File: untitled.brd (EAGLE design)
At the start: 95.2 x 57.4 mm, 62 parts, among them IC1 SIM900, IC2 ST1S10PHR, IC3 SMF05C, IC5 BQ24072, IC6 SIM68R, X1 ST-SMB-H, X2 ST-SMB-H

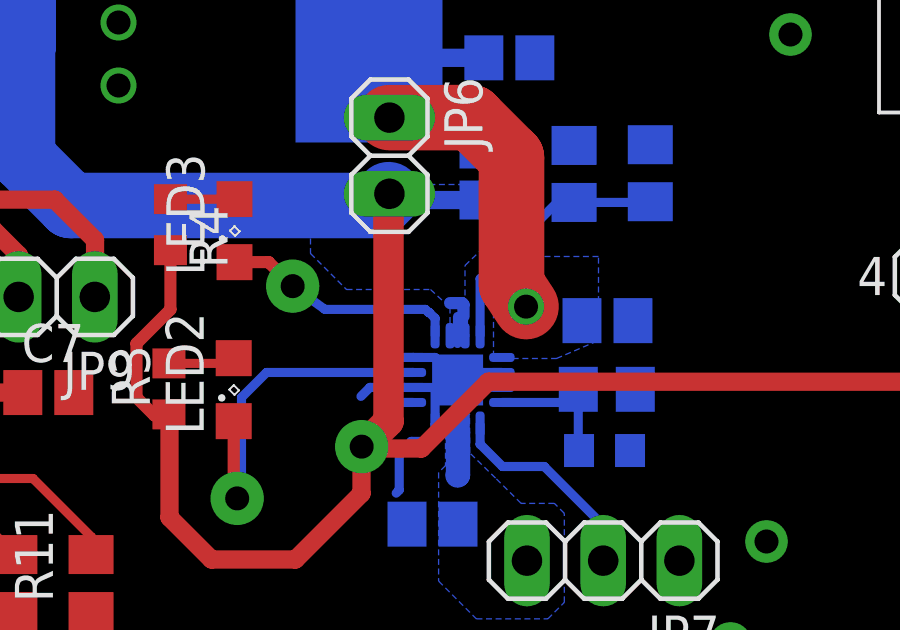
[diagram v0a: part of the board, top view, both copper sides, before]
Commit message: Supply changes
Some traces had been changed in power supply circuit
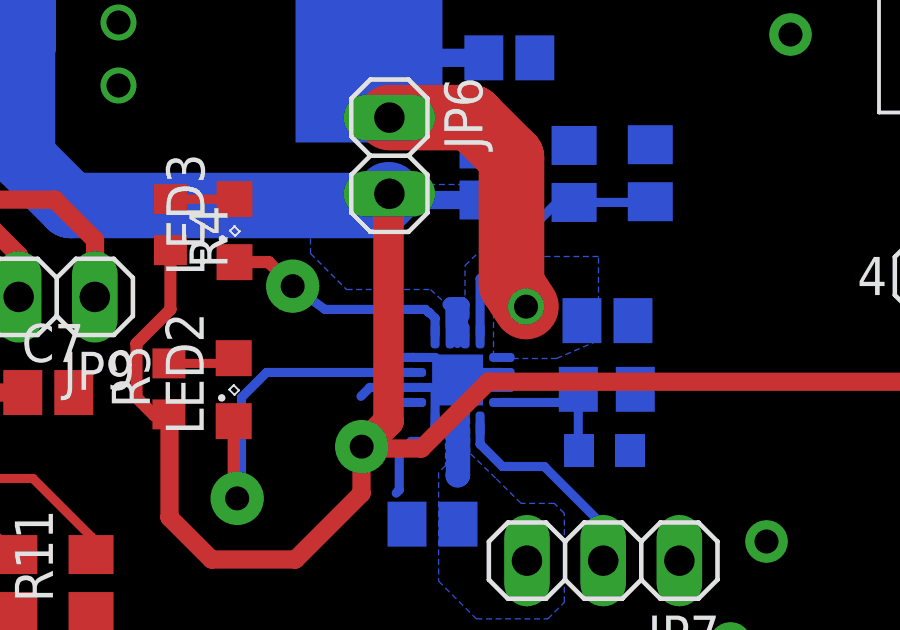
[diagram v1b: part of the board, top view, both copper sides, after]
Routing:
- net VBAT: track 150.0 -> 150.8 mm
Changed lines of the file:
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@@
 <wire x1="52" y1="13" x2="52" y2="14.556" width="0.6096" layer="1"/>
 <wire x1="52" y1="14.556" x2="52.006" y2="14.562" width="0.6096" layer="1"/>
-<wire x1="52.906" y1="22.962" x2="52.9" y2="22.9" width="0" layer="19" extent="1-16"/>
-<wire x1="52.931" y1="22.9895" x2="52.906" y2="22.962" width="0" layer="19" extent="16-16"/>
 <wire x1="54.9535" y1="19.3465" x2="55.3535" y2="19.3465" width="0.4064" layer="16"/>
 <wire x1="55.3535" y1="19.3465" x2="55.4" y2="19.3" width="0.4064" layer="16"/>
@@
 <wire x1="55.4535" y1="18.2595" x2="55.4" y2="18.2595" width="0.3048" layer="16"/>
 <wire x1="55.4" y1="18.2595" x2="55.4" y2="18.9" width="0.3048" layer="16"/>
+<wire x1="54.9" y1="19.3" x2="55" y2="19.3" width="0.4064" layer="16"/>
+<wire x1="55" y1="19.3" x2="55" y2="18.6" width="0.4064" layer="16"/>
+<wire x1="55" y1="18.6" x2="54.9535" y2="18.2595" width="0" layer="19" extent="16-16"/>
+<wire x1="52.906" y1="22.962" x2="52.931" y2="22.9895" width="0" layer="19" extent="16-16"/>
+<wire x1="52.9" y1="22.9" x2="52.906" y2="22.962" width="0" layer="19" extent="1-16"/>
 </signal>
 <signal name="N$5">

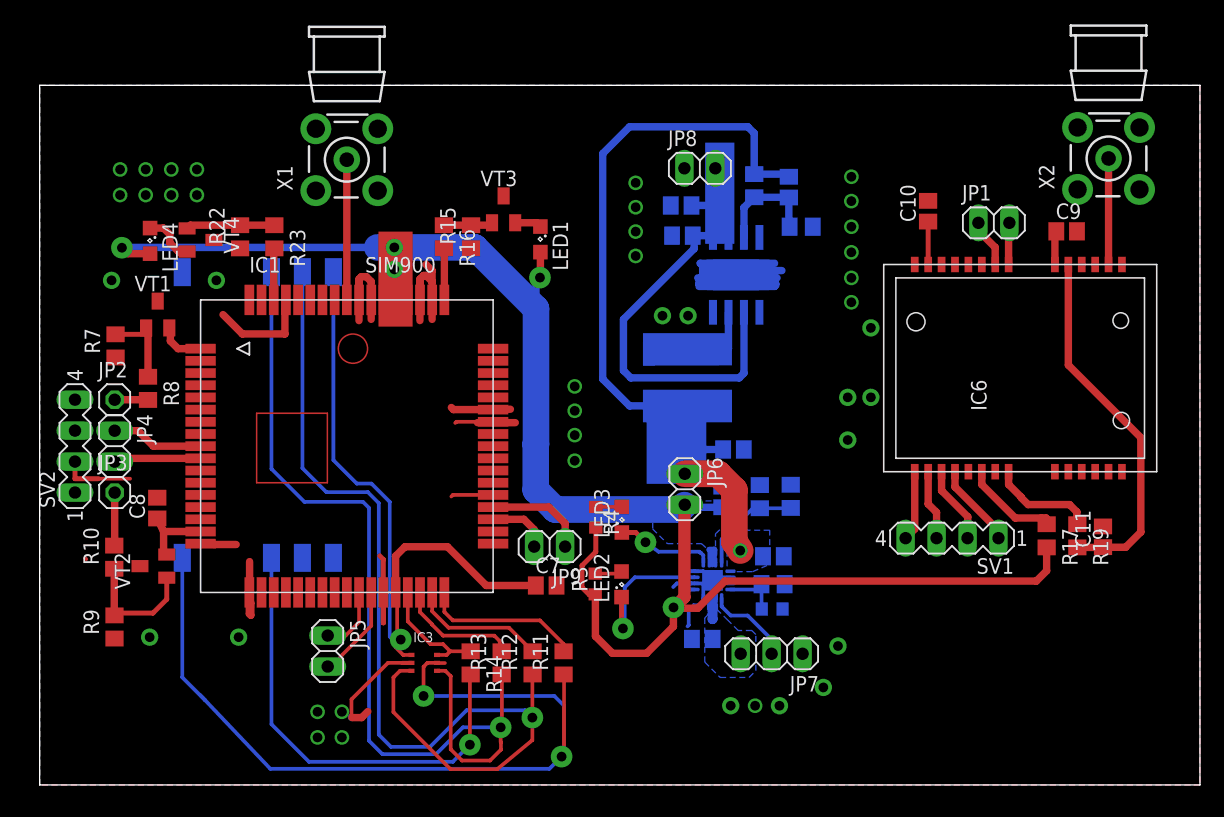
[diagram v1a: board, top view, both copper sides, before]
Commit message: Trace changes
Following items are changed:
- area between SIM900R and SIM68R footprints is restricted for placing
traces;
- some small changes in polygons around SIM900R;
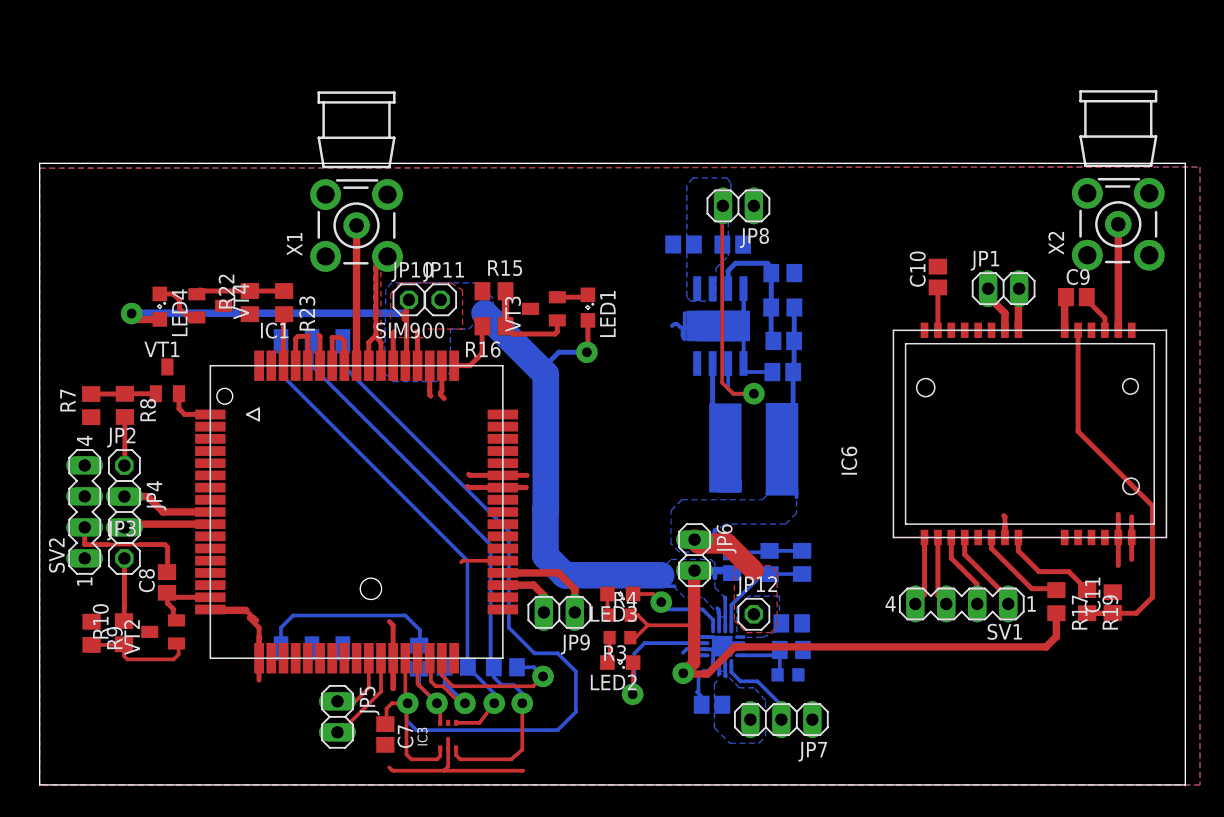
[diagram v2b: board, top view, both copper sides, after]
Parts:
- removed R11: 22, rcl:R0805
- removed SIM1: 912283001, con-molex-sim:91228-3001
- added JP10, JP11, JP12: (no value), pinhead:1X01
- added SIM2: ICA-501, ICA-501:ICA-501-006-F7
- moved C7 18.0 mm to (28.4, 4.14), turned to 270 degrees
- moved C4 12.6 mm to (61.0, 36.4), turned to 0 degrees
- moved R1 10.3 mm to (61.0, 39.2), turned to 180 degrees
- moved VT3 8.81 mm to (41.4, 39.1), turned to 90 degrees
- moved R16 8.41 mm to (37.3, 37.6), turned to 180 degrees
- moved R4 8.28 mm to (47.6, 13.9), turned to 0 degrees
- moved L1 7.92 mm to (58.6, 27.6), turned to 270 degrees
- moved C2 7.53 mm to (61.0, 33.9), turned to 0 degrees
- moved LED1 6.82 mm to (45.0, 39.2)
- moved LED2 6.42 mm to (47.6, 10.0), turned to 180 degrees
- moved IC3 6.28 mm to (33.5, 4.04), turned to 0 degrees
- moved R10 6.25 mm to (6.92, 12.5)
- moved C8 6.15 mm to (10.4, 16.6)
- moved LED3 6.10 mm to (47.6, 15.7), turned to 180 degrees
- moved C5 5.70 mm to (61.7, 13.3)
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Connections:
- removed net N$15: IC3.5, R11.1, SIM1.C8
- net +4.8V: now also JP12.1
- net GND: now also SIM2.GND; no longer SIM1.C4, SIM1.C5
- net N$14: now also SIM2.RESET; no longer SIM1.C2
- net N$17: now also SIM2.DATA; no longer SIM1.C7
- net N$18: now also SIM2.CLOCK; no longer SIM1.C3
- net SIM_PRESENCE: no longer R11.2
- net SIM_VDD: now also SIM2.VCC; no longer SIM1.C1
- net VBAT: now also JP10.1, JP11.1
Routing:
- net N$15: track 71.8 -> 0.00 mm, vias 2 -> 0
- net +4.8V: track 64.9 -> 26.7 mm, vias 1 -> 0
- net N$18: track 75.1 -> 41.0 mm
- net N$14: track 81.2 -> 48.3 mm
- net GND: track 121.5 -> 145.3 mm, vias 41 -> 0
- net N$17: track 37.6 -> 15.4 mm, vias 1 -> 0
- net +12V: track 39.6 -> 21.9 mm, vias 0 -> 1
- net SIM_VDD: track 57.3 -> 71.0 mm
- net SIM_PRESENCE: track 13.1 -> 0.00 mm
- net VBAT: track 150.8 -> 140.9 mm, vias 4 -> 3
- net N$19: track 4.03 -> 8.40 mm
- net N$47: track 4.00 -> 0.00 mm, vias 1 -> 0
- net N$3: track 8.92 -> 11.5 mm
- net SIM_RST: track 11.1 -> 13.3 mm, vias 0 -> 1
- net N$23: track 30.7 -> 32.4 mm
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- added copper zone on layer 16, net +12V
- added copper zone on layer 1, net +4.8V
- added copper zone on layer 1, net VBAT
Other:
- board size 95.2 x 57.4 mm -> 94 x 51 mm

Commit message: ST1S10 layout
Supply component's location has been changed due to ST1S10 datasheet
layout considerations
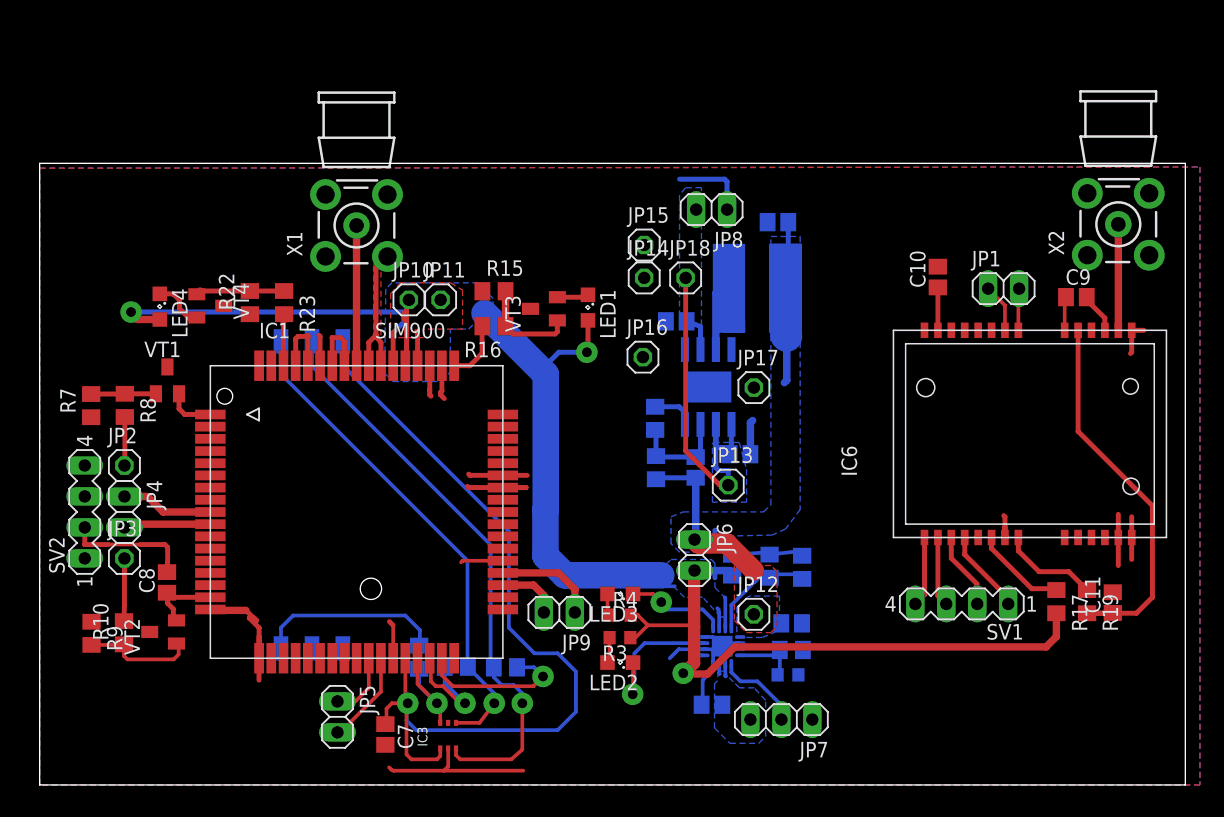
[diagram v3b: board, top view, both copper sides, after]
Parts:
- added JP13, JP14, JP15, JP16, JP17, JP18: (no value), pinhead:1X01
- moved C3 17.2 mm to (57.5, 27.1)
- moved R1 16.8 mm to (50.6, 26.0), turned to 270 degrees
- moved R2 15.9 mm to (50.5, 30.1), turned to 270 degrees
- moved L1 13.1 mm to (58.9, 40.8)
- moved C4 12.6 mm to (53.8, 26.1), turned to 90 degrees
- moved C2 12.3 mm to (60.6, 46.2)
- moved C1 6.33 mm to (52.2, 38.0)
- moved IC2 5.10 mm to (54.9, 32.6), turned to 0 degrees
- moved JP8 2.22 mm to (55.1, 47.2)
- moved R6 0.40 mm to (62.6, 17.9)
- moved R21 0.30 mm to (59.9, 18.0)
- moved C12 0.20 mm to (56.8, 18.0)
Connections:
- net +12V: now also JP13.1, JP18.1
- net GND: now also IC2.GND, JP14.1, JP15.1, JP16.1, JP17.1
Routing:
- net +12V: track 21.9 -> 32.9 mm
- net GND: track 145.3 -> 135.2 mm
- net VBAT: track 140.9 -> 145.6 mm
- net +4.8V: track 26.7 -> 29.3 mm
- net N$3: track 11.5 -> 9.13 mm
- net N$1: track 7.37 -> 5.80 mm
- net N$6: track 8.91 -> 9.64 mm

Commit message: SeedStudio preparation
GSM fotprint, polygons, thermals
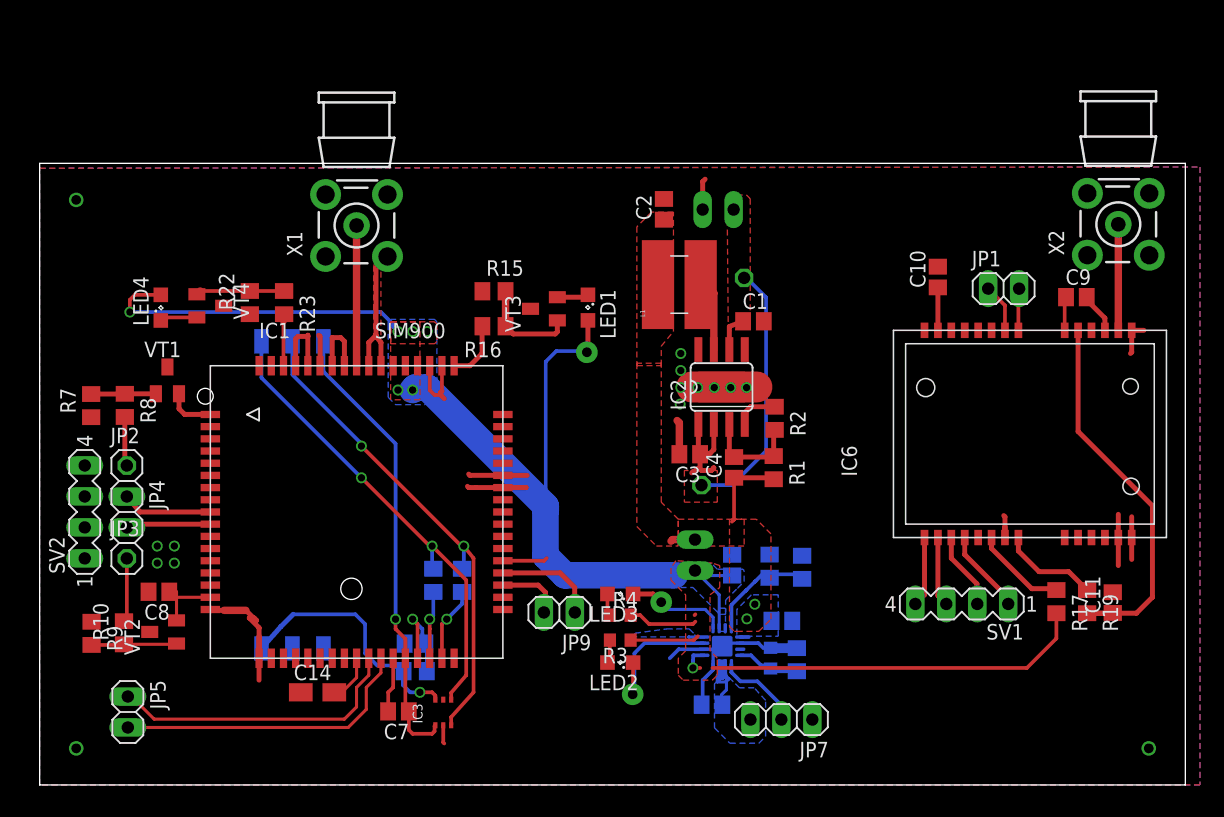
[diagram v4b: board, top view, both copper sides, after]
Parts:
- removed JP10, JP11, JP12, JP14, JP15, JP16, JP17: (no value), pinhead:1X01
- added C13: 18p, resistor:C0805
- added C14: (no value), rcl:A/3216-18R
- C7: value 4.7u -> 100n
- L1: device CDRH6D38:INDUCTOR-SUMIDA-CDRH4D18 -> inductor-sumida-cdrh4d18:INDUCTOR-SUMIDA-CDRH4D18
- moved JP5 17.2 mm to (7.24, 5.99)
- moved R2 9.80 mm to (60.3, 30.1), flipped to the top
- moved R1 9.66 mm to (60.2, 26.0), flipped to the top
- moved C2 9.41 mm to (51.2, 47.2), flipped to the top, turned to 90 degrees
- moved R12 7.97 mm to (34.7, 16.8), turned to 270 degrees
- moved R13 7.33 mm to (32.3, 16.8), turned to 270 degrees
- moved L1 6.41 mm to (52.5, 41.0), flipped to the top, turned to 90 degrees
- moved C1 6.33 mm to (58.6, 38.0), flipped to the top
- moved JP18 4.80 mm to (57.8, 41.6), flipped to the bottom
- moved C3 4.13 mm to (53.3, 27.1), flipped to the top
- moved C4 3.14 mm to (57.0, 26.1), flipped to the top
- moved JP13 2.20 mm to (54.3, 24.6), flipped to the bottom
- moved C7 2.18 mm to (29.4, 6.04), turned to 180 degrees
- moved R5 1.98 mm to (60.0, 10.4), turned to 270 degrees
- moved IC3 1.94 mm to (33.1, 5.95)
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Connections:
- new net N$15: IC3.6, R14.2, SIM2.DATA
- net +4.8V: no longer JP12.1
- net GND: now also C13.2, C14.-; no longer JP14.1, JP15.1, JP16.1, JP17.1
- net N$17: now also C14.+, IC1.26; no longer R14.2, SIM2.DATA
- net SIM_DATA: now also C13.1; no longer IC3.6
- net VBAT: no longer JP10.1, JP11.1
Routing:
- net SIM_VDD: track 71.0 -> 37.6 mm
- net GND: track 135.2 -> 113.7 mm, vias 0 -> 15
- net N$15: track 0.00 -> 20.7 mm, vias 0 -> 1
- net DBG_TXD: track 5.47 -> 24.4 mm
- net +4.8V: track 29.3 -> 10.8 mm, vias 0 -> 2
- net DBG_RXD: track 7.72 -> 24.9 mm
- net VBAT: track 145.6 -> 133.6 mm, vias 3 -> 8
- net N$17: track 15.4 -> 3.92 mm
- net BAT: track 1.86 -> 10.2 mm
- net N$14: track 48.3 -> 40.4 mm, vias 1 -> 2
- net SIM_RST: track 13.3 -> 6.12 mm
- net SIM_CLK: track 9.17 -> 5.56 mm
- net +12V: track 32.9 -> 35.4 mm, vias 1 -> 0
- net N$12: track 9.37 -> 7.02 mm
- net N$18: track 41.0 -> 38.8 mm, vias 1 -> 2
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- added copper zone on layer 1, net +12V
- removed copper zone on layer 16, net +12V

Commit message: BQ now on the top
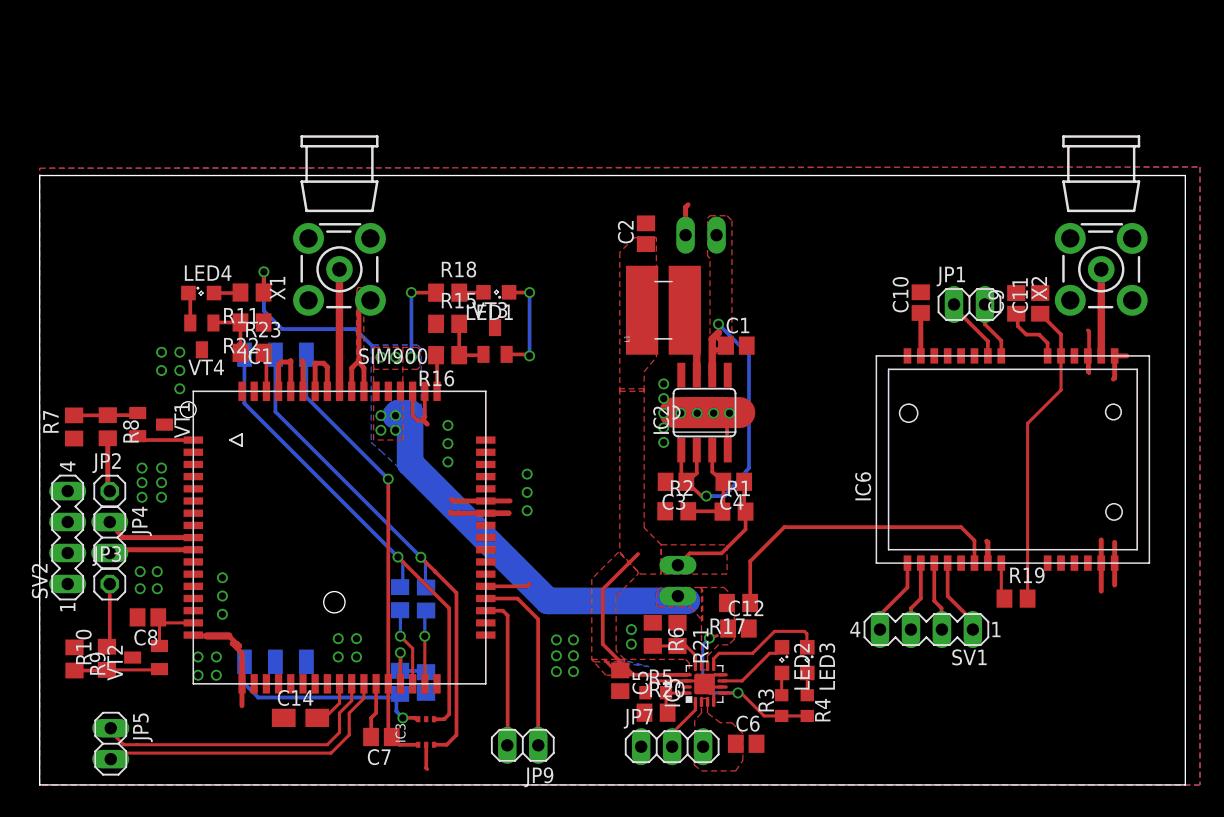
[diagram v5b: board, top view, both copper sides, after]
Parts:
- removed JP13, JP18: (no value), pinhead:1X01
- added R11, R18: 150, rcl:R0805
- moved R17 26.1 mm to (57.3, 14.9), turned to 180 degrees
- moved C11 25.3 mm to (82.1, 39.5)
- moved R4 17.0 mm to (63.0, 6.51), turned to 270 degrees
- moved LED3 16.3 mm to (63.0, 10.2), turned to 270 degrees
- moved R3 14.3 mm to (60.9, 6.51), turned to 90 degrees
- moved C5 14.1 mm to (47.6, 8.55), flipped to the top, turned to 270 degrees
- moved R6 13.4 mm to (50.3, 12.4), flipped to the top
- moved LED2 13.3 mm to (60.9, 10.2), turned to 270 degrees
- moved R20 12.3 mm to (50.6, 5.93), flipped to the top, turned to 0 degrees
- moved JP9 11.3 mm to (39.6, 3.25)
- moved R2 11.1 mm to (52.3, 22.5), turned to 0 degrees
- moved R5 9.84 mm to (50.5, 7.57), flipped to the top, turned to 0 degrees
- moved R21 9.40 mm to (52.3, 12.4), flipped to the top
- moved JP7 9.23 mm to (51.9, 3.14), turned to 0 degrees
- moved LED1 7.62 mm to (37.5, 40.4), turned to 180 degrees
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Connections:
- new net N$36: LED4.A, R11.2
- new net N$45: LED1.A, R18.2
- net +12V: no longer JP13.1, JP18.1
- net VBAT: now also R11.1, R18.1; no longer LED1.A, LED4.A
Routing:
- net VBAT: track 133.6 -> 77.5 mm, vias 8 -> 11
- net +4.8V: track 10.8 -> 34.4 mm, vias 2 -> 0
- net N$21: track 7.63 -> 25.3 mm
- net BAT: track 10.2 -> 0.00 mm
- net GND: track 113.7 -> 105.6 mm, vias 15 -> 49
- net N$23: track 32.4 -> 25.2 mm
- net N$34: track 5.44 -> 12.6 mm
- net N$33: track 8.44 -> 15.3 mm
- net N$9: track 12.3 -> 6.02 mm, vias 1 -> 0
- net N$16: track 2.59 -> 8.83 mm, vias 0 -> 2
- net N$22: track 8.07 -> 3.02 mm
- net N$6: track 9.64 -> 4.69 mm
- net N$19: track 8.40 -> 4.59 mm
- net N$14: track 40.4 -> 43.4 mm, vias 2 -> 1
- net +12V: track 35.4 -> 32.6 mm, vias 0 -> 2
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- added copper zone on layer 1, net BAT
- removed copper zone on layer 16, net +4.8V
- removed copper zone on layer 16, net BAT
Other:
- board size 94 x 51 mm -> 94 x 50 mm
